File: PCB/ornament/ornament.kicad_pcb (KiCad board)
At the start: 2 copper layers, 40 x 40 mm, 40 parts, among them J1 USB_B_Micro, J3 Conn_01x06, SW1 MODE, U1 PIC16F18325-ISL

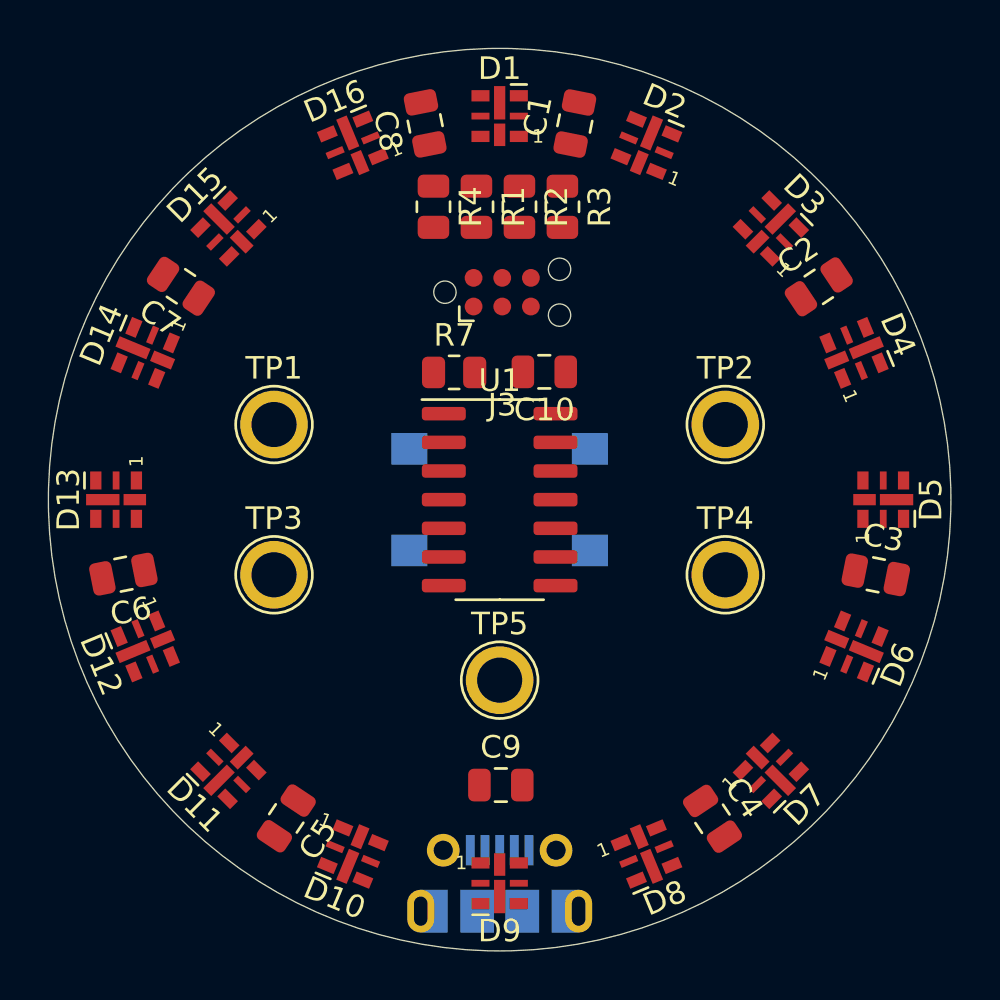
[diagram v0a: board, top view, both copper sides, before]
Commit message: routed PCB, about to upgrade kicad
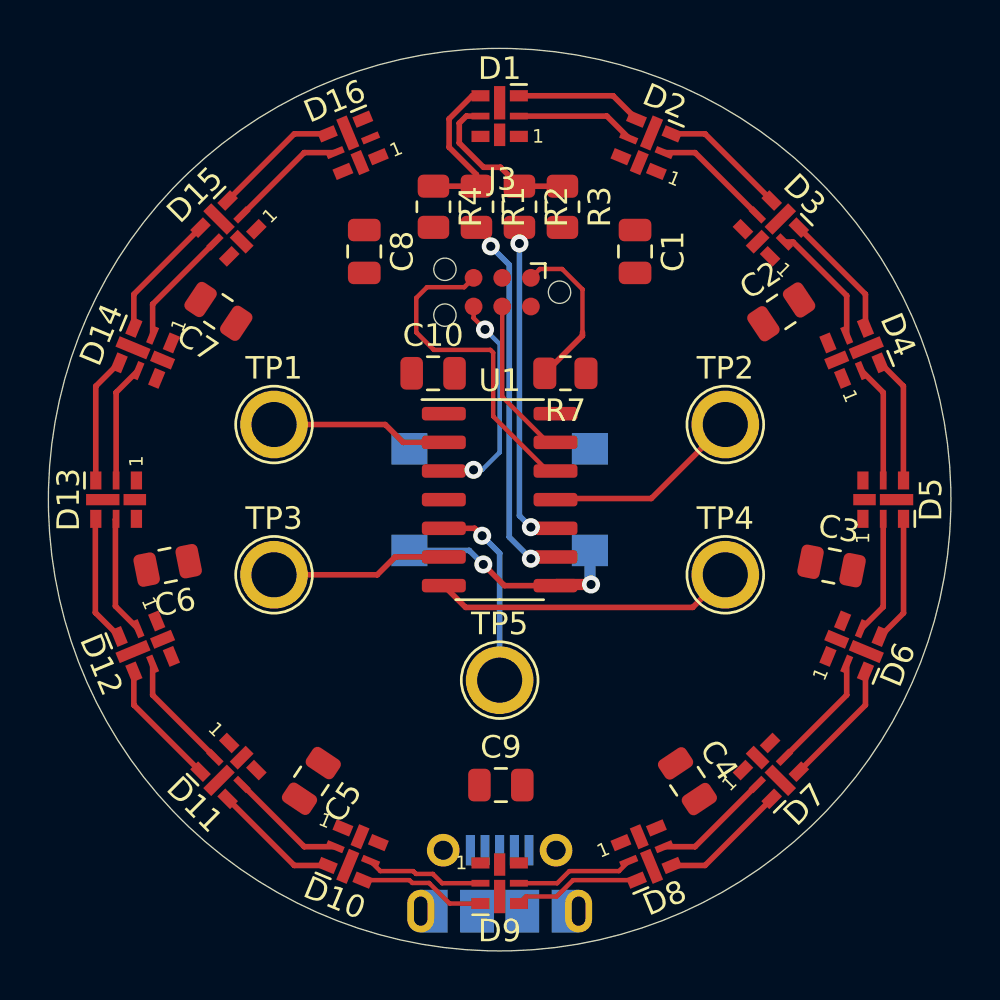
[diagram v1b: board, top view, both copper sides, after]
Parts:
- moved C8 6.28 mm to (144.0, 89.0), turned to 270 degrees
- moved C1 6.27 mm to (156.0, 89.0), turned to 270 degrees
- moved R7 4.93 mm to (152.9, 94.4), turned to 180 degrees
- moved C10 4.93 mm to (147.1, 94.4), turned to 0 degrees
- moved C2 2.00 mm to (162.5, 91.7)
- moved C4 2.00 mm to (158.3, 112.5)
- moved C3 2.00 mm to (164.7, 102.9)
- moved C6 2.00 mm to (135.3, 102.9)
- moved C7 2.00 mm to (137.5, 91.7)
- moved C5 2.00 mm to (141.7, 112.5)
- turned J3 to 180 degrees
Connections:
- U1 pad 5: Net-(TP4-Pad1) -> Net-(TP5-Pad1)
- U1 pad 7: Net-(TP5-Pad1) -> Net-(TP4-Pad1)
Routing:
- net /DATA: track 0.00 -> 16.8 mm, vias 0 -> 2
- net /CLK: track 0.00 -> 15.0 mm, vias 0 -> 2
- net Net-(J3-Pad5): track 0.00 -> 14.8 mm
- net Net-(TP4-Pad1): track 0.00 -> 13.5 mm
- net /MODE: track 0.00 -> 10.2 mm, vias 0 -> 2
- net Net-(J3-Pad6): track 0.00 -> 9.76 mm, vias 0 -> 2
- net Net-(TP2-Pad1): track 0.00 -> 8.90 mm
- net Net-(TP5-Pad1): track 0.00 -> 8.56 mm, vias 0 -> 1
- net Net-(TP3-Pad1): track 0.00 -> 7.85 mm
- net Net-(TP1-Pad1): track 0.00 -> 7.85 mm
- net Net-(D1-Pad5): track 0.00 -> 7.32 mm
- net Net-(J3-Pad1): track 0.00 -> 7.24 mm
- net Net-(D1-Pad4): track 0.00 -> 7.20 mm
- net Net-(J3-Pad4): track 0.00 -> 7.20 mm
- net Net-(D12-Pad3): track 0.00 -> 5.66 mm
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
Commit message: Update documentation, update firmware, add gerbers
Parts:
- added G***: LOGO, LOGO, F.Cu at (144.0, 109.0)
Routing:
- net GND: track 0.13 -> 67.7 mm, vias 0 -> 35
- net Net-(J3-Pad1): track 7.24 -> 23.9 mm, vias 0 -> 2
- net +5V: track 0.00 -> 14.2 mm, vias 0 -> 3
- net Net-(D12-Pad3): track 5.66 -> 0.00 mm
- net Net-(D6-Pad3): track 5.64 -> 0.00 mm
- net Net-(D3-Pad3): track 5.64 -> 0.00 mm
- net Net-(D14-Pad3): track 5.64 -> 0.00 mm
- net Net-(D11-Pad3): track 5.64 -> 0.00 mm
- net Net-(D7-Pad3): track 5.64 -> 0.00 mm
- net Net-(D15-Pad3): track 5.64 -> 0.00 mm
- net Net-(D10-Pad3): track 5.64 -> 0.00 mm
- net Net-(D5-Pad3): track 5.64 -> 0.00 mm
- net Net-(D4-Pad3): track 5.64 -> 0.00 mm
- net Net-(D13-Pad3): track 5.64 -> 0.00 mm
- net Net-(D1-Pad3): track 5.64 -> 0.00 mm
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- added copper zone on F.Cu, net +5V
- added copper zone on B.Cu, net GND
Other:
- net class Default removed
- board text added: "JLCJLCJLCJLC"
- board text added: "ZACH MARTIN LED RING V1 8-22"
